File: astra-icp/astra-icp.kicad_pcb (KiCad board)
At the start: 2 copper layers, 180 x 56 mm, 70 parts, among them IC1 ATA6561-GAQW-N, J1 PINHD_1x5_Male, J2 PWR_IN, J3 CAN_TERMINAL, SW1 CHOC_HS, SW10 CHOC_HS, SW11 CHOC_HS, SW12 CHOC_HS, SW13 CHOC_HS, SW14 CHOC_HS, SW15 CHOC_HS, SW16 CHOC_HS, SW17 CHOC_HS, SW18 CHOC_HS, SW19 CHOC_HS, SW2 CHOC_HS, SW20 CHOC_HS, SW3 CHOC_HS, SW4 CHOC_HS, SW5 CHOC_HS, SW6 CHOC_HS, SW7 CHOC_HS, SW8 CHOC_HS, SW9 CHOC_HS, U3 STM32F042C4Tx

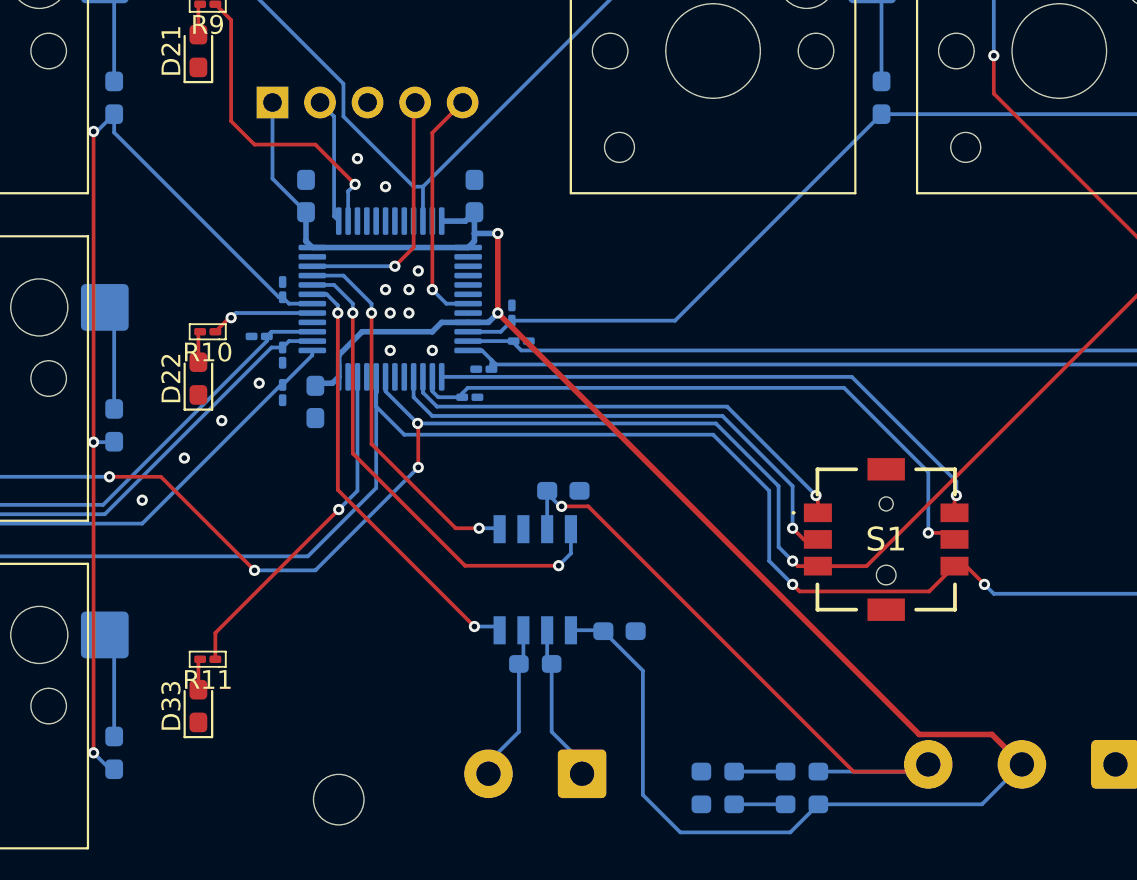
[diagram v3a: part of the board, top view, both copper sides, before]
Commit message: feat: Corrected most errors in ICP DRC
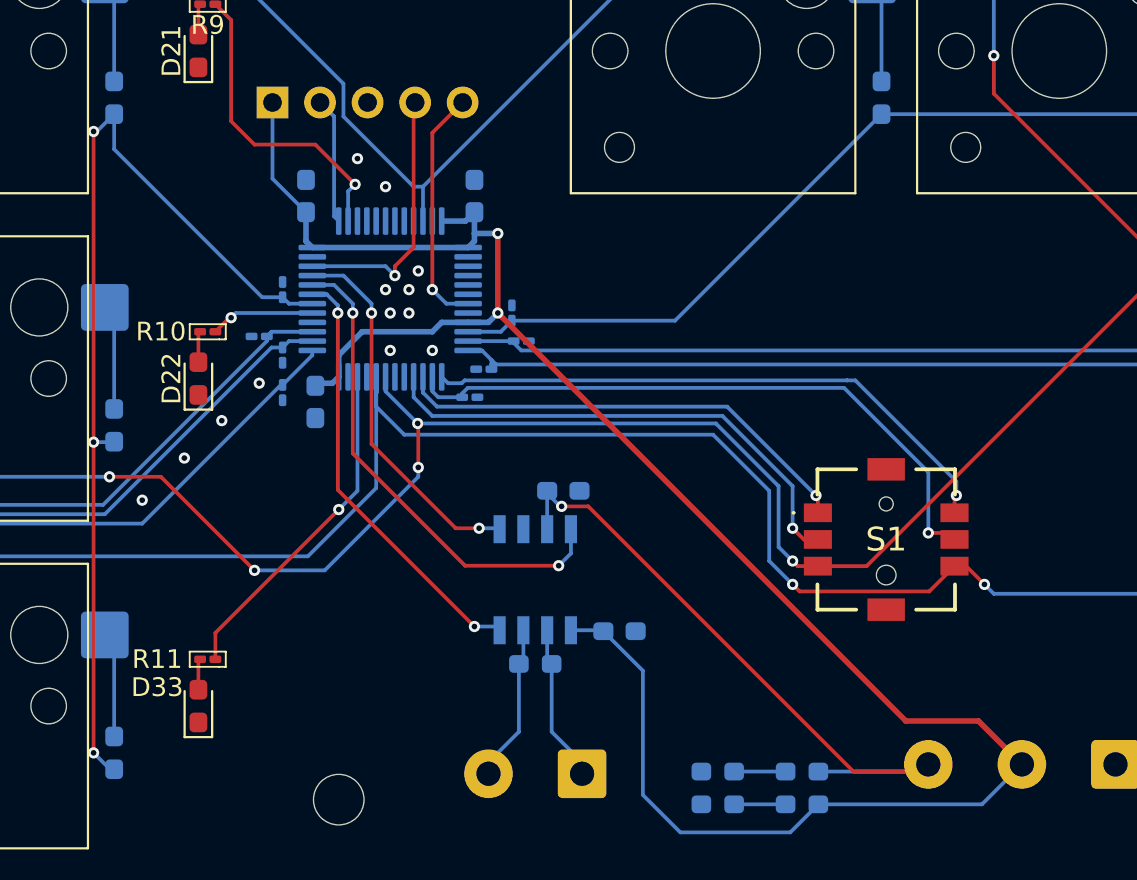
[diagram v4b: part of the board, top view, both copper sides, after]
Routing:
- net SWDIO: track 13.6 -> 14.3 mm
- net COL3: track 52.6 -> 53.1 mm

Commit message: feat: Final work on ICP PCB
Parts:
- added J4: UART, Connector_PinHeader_2.54mm:PinHeader_1x02_P2.54mm_Vertical, B.Cu at (116.6, 31.0)
- J1: value PINHD_1x5_Male -> SWD
- moved R3 0.25 mm to (108.0, 47.8)
- moved S1 0.15 mm to (141.9, 58.6), turned to 45 degrees
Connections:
- U3 pad 42: unconnected-(U3-PB6-Pad42) -> UART_TX
- U3 pad 43: unconnected-(U3-PB7-Pad43) -> UART_RX
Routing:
- net UART_TX: track 0.00 -> 13.3 mm, vias 0 -> 1
- net UART_RX: track 0.00 -> 12.4 mm, vias 0 -> 1
- net ROW1: track 216.3 -> 222.9 mm
- net ROW4: track 27.2 -> 31.5 mm
- net ROW3: track 31.7 -> 27.6 mm
- net COL7: track 34.4 -> 30.9 mm
- net ROW5: track 25.1 -> 28.1 mm
- net ROW2: track 182.7 -> 180.3 mm
- net +3V3: track 110.8 -> 111.3 mm
- net GND: vias 15 -> 613
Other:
- board text added: "3V3"
- board text added: "5V"
- board text added: "ALP"
- board text added: "ANF"
- board text added: "GND"
- board text added: "H"
- board text added: "L"
- board text added: "NRST"
- board text added: "NUM"
- board text added: "RX"
- board text added: "SWCLK"
- board text added: "SWDIO"
- board text added: "TX"

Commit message: feat: Added missing board name and revision
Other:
- board text added: "Astra OS ICP Board rev 1 by Didas72"
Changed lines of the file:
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@@
+		)
+	)
+	(gr_text "Astra OS ICP Board\nrev 1 by Didas72"
+		(at 161.75 56.5 0)
+		(layer "B.SilkS")
+		(effects
+			(font
+				(size 1 1)
+				(thickness 0.1)
+			)
+			(justify left bottom mirror)
 		)
 	)

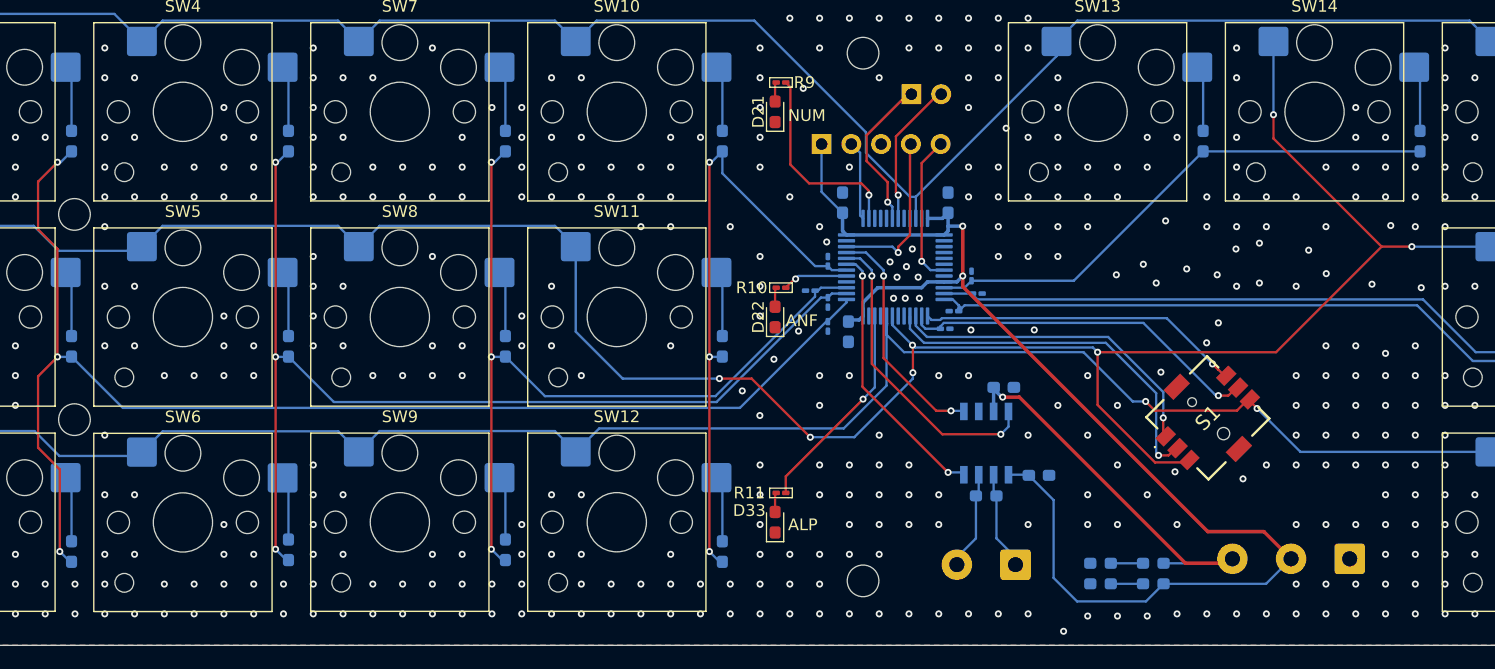
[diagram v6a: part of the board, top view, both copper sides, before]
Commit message: feat: Changed resistors to 0603
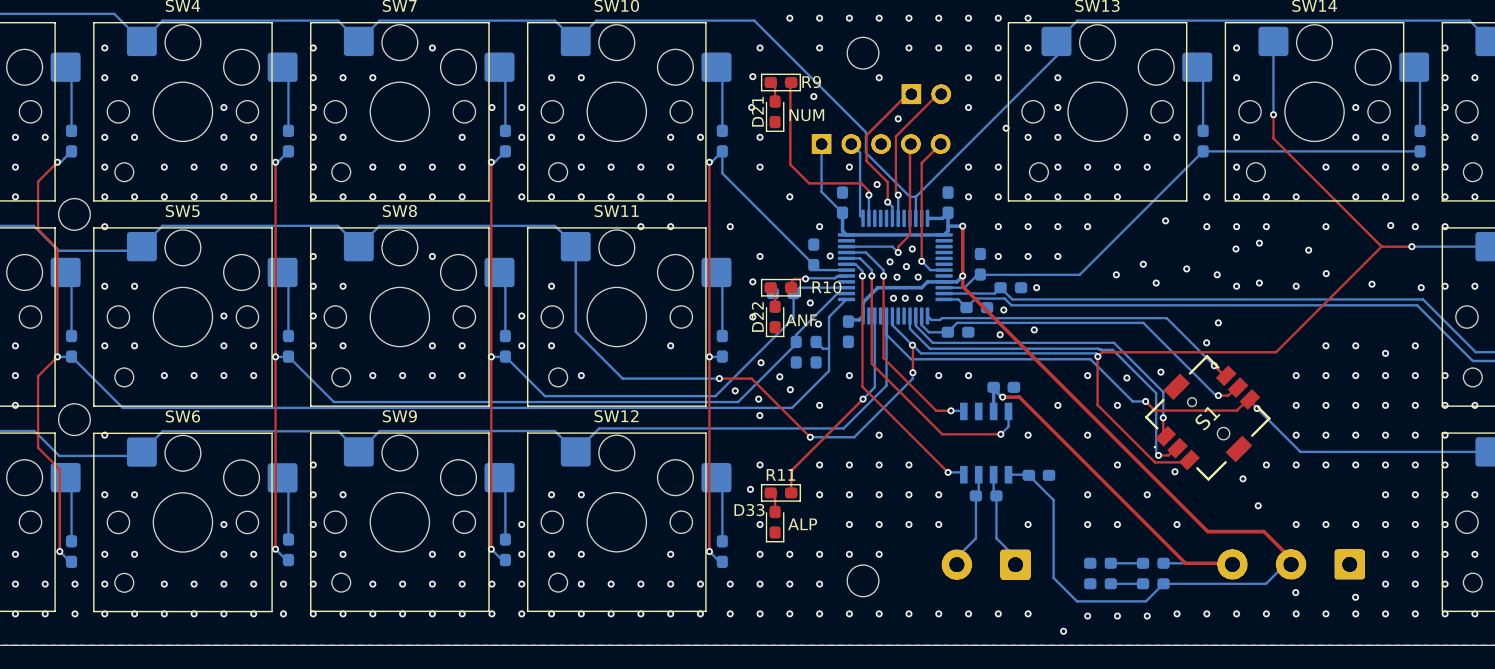
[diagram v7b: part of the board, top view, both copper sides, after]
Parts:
- R1, R10, R11, R2, R3, R4, R5, R6, R7, R8, R9: footprint PCM_Resistor_SMD_AKL:R_0201_0603Metric_Pad0.64x0.40mm_HandSolder -> PCM_Resistor_SMD_AKL:R_0603_1608Metric_Pad1.05x0.95mm_HandSolder
- moved R2 5.04 mm to (106.8, 53.0)
- moved R6 2.89 mm to (125.1, 47.5)
- moved R1 2.42 mm to (108.5, 53.0)
- moved R3 2.31 mm to (105.7, 48.0)
- moved R7 1.97 mm to (122.2, 49.2), turned to 180 degrees
- moved R4 1.32 mm to (108.3, 44.7)
- moved R5 1.25 mm to (122.5, 45.5)
- moved R8 1.14 mm to (120.6, 51.3)
- moved J2 0.48 mm to (154.0, 71.1)
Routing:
- net COL0: track 112.1 -> 115.9 mm
- net COL2: track 72.0 -> 72.9 mm
- net COL6: track 125.0 -> 124.3 mm
- net GND: vias 613 -> 621
